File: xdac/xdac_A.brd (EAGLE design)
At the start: 100 x 80 mm, 76 parts, among them J1 LIWE_40_PIN, J12 FC68131, J3 PINHD-3X9/90, J34 FC68131, J4 PINHD-3X5/90, J56 FC68131, J78 FC68131, U1 STA311B, U2 CS4384, U3 FIN1002

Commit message: xdac: VIP
Signed-off-by: malo <pavol.malosek@gmail.com>
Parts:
- removed CKOUT, MUTEC_1, MUTEC_234: TPB1,27, testpad:B1,27
- removed J4: PINHD-3X5/90, 25pinhead:3X05/90
- removed R1: 220R, rcl:R0603
- removed R2, R3, R4, R5, R6: 470R, rcl:R0603
- removed U1: STA311B, 25cmsquare:VFQFPN_56_8X8
- C11, C12, C13, C14, C17, C18, C23, C24: device 25cmsquare:EEE-FC1V220P -> 25cmsquare:EEE-FC1C220R
- C15, C16, C19, C2, C20, C21, C22, C25, C26, C8, C9: device rcl:C0603K -> rcl:C0603
- J2: value (none) -> PINHD-3X5/90; device 25pinhead:3X08/90 -> 25pinhead:3X05/90
- J3: value PINHD-3X9/90 -> PINHD-3X5/90; device 25pinhead:3X9/90 -> 25pinhead:3X05/90
- moved R24 209.5 mm to (66.8, 20.1)
- moved C22 209.0 mm to (67.8, 30.5), turned to 270 degrees
- moved C21 204.2 mm to (67.8, 33.5), turned to 90 degrees
- moved R21 200.1 mm to (66.8, 27.9)
- moved R20 190.7 mm to (66.8, 36.1)
- moved C20 188.9 mm to (67.8, 62.5), turned to 270 degrees
- moved C16 188.1 mm to (67.8, 46.5), turned to 270 degrees
- moved C19 184.2 mm to (67.8, 65.5), turned to 90 degrees
- moved C15 183.4 mm to (67.8, 49.5), turned to 90 degrees
- moved R17 181.5 mm to (66.8, 43.9)
- moved C14 179.4 mm to (60.6, 45.1)
- moved R16 172.3 mm to (66.8, 52.1)
- moved R27 168.5 mm to (65.8, 14.5), turned to 270 degrees
- moved C13 167.9 mm to (60.6, 50.9)
- moved R13 163.4 mm to (66.8, 59.9)
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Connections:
- net CS_AOUT1 renamed AOUT1
- net CS_AOUT2 renamed AOUT2
- net CS_AOUT3 renamed AOUT3
- net CS_AOUT4 renamed AOUT4
- net CS_AOUT5 renamed AOUT5
- net CS_AOUT6 renamed AOUT6
- net CS_AOUT7 renamed AOUT7
- net CS_AOUT8 renamed AOUT8
- net N$13 renamed AUOT1_
- net N$14 renamed AOUT2_
- net N$23 renamed FILT+
- net N$25 renamed AOUT4_
- net N$26 renamed VQ
- net N$29 renamed AOUT3_
- net N$32 renamed AOUT6_
- net N$35 renamed AOUT5_
- net N$38 renamed AOUT8_
- net N$41 renamed AOUT7_
- removed net CS_DSD1: J2.10, U2.3
- removed net CS_DSD2: J2.12, U2.2
- removed net CS_DSD3: J2.13, U2.1
- removed net CS_DSD4: J2.15, U2.48
- removed net CS_DSD5: J2.16, U2.47
- removed net CS_DSD6: J2.18, U2.46
- removed net CS_DSD7: J2.19, U2.45
- removed net CS_DSD8: J2.21, U2.44
- removed net CS_DSD_CLK: J2.22, U2.42
- removed net CS_LRCLK: J2.3, R2.2, U2.7
- removed net CS_RST_N: J2.24, U2.19
- removed net CS_SCLK: J2.1, R1.2, U2.9
- removed net CS_SDIN1: J2.4, R3.2, U2.8
- removed net CS_SDIN2: J2.6, R4.2, U2.11
- removed net CS_SDIN3: J2.7, R5.2, U2.13
- removed net CS_SDIN4: J2.9, R6.2, U2.14
- removed net N$1: R1.1, U1.48
- removed net N$10: CKOUT.TP, U1.22
- removed net N$2: R2.1, U1.49
- removed net N$3: R3.1, U1.50
- removed net N$31: J4.15
- removed net N$4: R4.1, U1.51
- removed net N$43: J3.27
- removed net N$5: R5.1, U1.54
- removed net N$6: R6.1, U1.55
- removed net N$8: MUTEC_1.TP, U2.41
- removed net N$9: MUTEC_234.TP, U2.22
- removed net STA_1A: J3.1, U1.44
- removed net STA_1B: J3.3, U1.43
- removed net STA_2A: J3.4, U1.42
- removed net STA_2B: J3.6, U1.41
- removed net STA_3A: J3.7, U1.38
- removed net STA_3B: J3.9, U1.37
- removed net STA_4A: J3.10, U1.36
- removed net STA_4B: J3.12, U1.35
- removed net STA_5A: J3.13, U1.34
- removed net STA_5B: J3.15, U1.33
- removed net STA_6A: J3.16, U1.30
- removed net STA_6B: J3.18, U1.29
- removed net STA_7A: J3.19, U1.28
- removed net STA_7B: J3.21, U1.27
- removed net STA_8A: J3.22, U1.26
- removed net STA_8B: J3.24, U1.25
- removed net STA_BICKI: J4.1, U1.10
- removed net STA_EAPD: J3.25, U1.45
- removed net STA_LRCKI: J4.3, U1.9
- removed net STA_MVO: J4.10, U1.1
- removed net STA_PWDN: J4.13, U1.56
- removed net STA_RST_N: J4.12, U1.13
- removed net STA_SDI12: J4.4, U1.8
- removed net STA_SDI34: J4.6, U1.7
- removed net STA_SDI56: J4.7, U1.6
- removed net STA_SDI78: J4.9, U1.5
- new net DSD1: J2.3, U2.3
- new net DSD2: J2.1, U2.2
- new net DSD3: J2.6, U2.1
- new net DSD4: J2.4, U2.48
- new net DSD5: J2.9, U2.47
- new net DSD6: J2.7, U2.46
- new net DSD7: J2.12, U2.45
- new net DSD8: J2.10, U2.44
- new net DSD_CLK: J2.15, U2.42
- new net LRCLK: J3.3, U2.7
- new net MUTEC_1: J2.13, U2.41
- new net MUTEC_234: J3.15, U2.22
- new net RST_N: J3.12, U2.19
- new net SCLK: J3.1, U2.9
- new net SDIN1: J3.4, U2.8
- new net SDIN2: J3.6, U2.11
- new net SDIN3: J3.7, U2.13
- new net SDIN4: J3.9, U2.14
- net +3V3: no longer U1.11, U1.24, U1.3, U1.31, U1.39, U1.46, U1.52
- net 3V3A: no longer U1.21
- net GND: no longer J2.17, J2.20, J2.23, J3.17, J3.20, J3.23, J3.26, J4.11, J4.14, J4.2, J4.5, J4.8, U1.12, U1.14, U1.15, U1.2, U1.20, U1.23, U1.32, U1.4, U1.40, U1.47, U1.53, U1.PAD
- net MCLK: no longer U1.18
- net SCL: no longer U1.17
- net SDA: no longer U1.16
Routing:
- net GND: track 0.00 -> 59.6 mm
- net DSD1: track 0.00 -> 39.9 mm
- net DSD3: track 0.00 -> 37.8 mm
- net DSD7: track 0.00 -> 35.9 mm
- net DSD5: track 0.00 -> 35.8 mm
- net DSD_CLK: track 0.00 -> 35.1 mm
- net DSD2: track 0.00 -> 33.4 mm
- net AOUT1: track 0.00 -> 31.2 mm
- net AOUT8: track 0.00 -> 30.7 mm
- net DSD8: track 0.00 -> 30.5 mm
- net DSD4: track 0.00 -> 30.4 mm
- net DSD6: track 0.00 -> 30.1 mm
- net MUTEC_1: track 0.00 -> 30.0 mm
- net AOUT7: track 0.00 -> 26.4 mm
- net AOUT2: track 0.00 -> 25.3 mm
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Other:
- board size 100 x 80 mm -> 80 x 80 mm

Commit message: xdac: WIP
Signed-off-by: malo <pavol.malosek@gmail.com>
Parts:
- added JP1, JP3: (no value), 25pinhead:1X02/90
- C10: value 47u, EEEFC1V470P -> 47u, EEEFC0J470R; device 25cmsquare:EEE-FC1V470P -> 25cmsquare:EEE-FC1C220R
- C4, C5: device rcl:C0603K -> rcl:C0603
- moved C3 37.6 mm to (53.7, 40.0), turned to 90 degrees
- moved C30 31.2 mm to (14.9, 31.4), turned to 270 degrees
- moved C4 30.4 mm to (47.0, 40.7)
- moved C9 14.5 mm to (41.2, 32.2), turned to 270 degrees
- moved C10 13.7 mm to (40.3, 27.3), turned to 270 degrees
- moved C32 10.4 mm to (16.3, 23.1)
- moved C31 9.97 mm to (11.4, 23.0)
- moved JP2 9.47 mm to (11.2, 47.9), turned to 90 degrees
- moved FB2 8.90 mm to (13.6, 22.2)
- moved C7 7.91 mm to (45.9, 27.3), turned to 270 degrees
- moved C34 7.67 mm to (16.3, 14.8), turned to 270 degrees
- moved C15 7.41 mm to (72.8, 55.0), turned to 180 degrees
- moved C22 7.41 mm to (72.8, 25.0), turned to 180 degrees
- moved C19 7.41 mm to (72.8, 71.0), turned to 180 degrees
- moved C25 7.41 mm to (72.8, 23.0), turned to 180 degrees
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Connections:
- net GND: now also JP1.1, JP3.1
- net MUTEC_1: now also JP3.2; no longer J2.13
- net MUTEC_234: now also JP1.2; no longer J3.15
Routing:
- net 5VA: track 0.00 -> 192.0 mm
- net 3V3A: track 0.00 -> 80.3 mm, vias 0 -> 2
- net GND: track 59.6 -> 6.40 mm
- net +2V5: track 0.00 -> 51.0 mm
- net RST_N: track 1.53 -> 42.6 mm, vias 0 -> 2
- net SDIN1: track 0.00 -> 37.6 mm, vias 0 -> 2
- net SCLK: track 0.00 -> 36.2 mm, vias 0 -> 2
- net LRCLK: track 1.31 -> 33.1 mm, vias 0 -> 2
- net SDIN2: track 0.00 -> 31.5 mm, vias 0 -> 2
- net SDA: track 0.00 -> 23.3 mm, vias 0 -> 2
- net MCLK: track 0.00 -> 22.1 mm, vias 0 -> 2
- net SDIN3: track 0.00 -> 21.9 mm, vias 0 -> 2
- net SDIN4: track 0.00 -> 21.4 mm, vias 0 -> 2
- net SCL: track 0.00 -> 20.4 mm, vias 0 -> 2
- net +3V3: track 0.00 -> 20.1 mm, vias 0 -> 2
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
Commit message: xdac: VIP
Signed-off-by: malo <pavol.malosek@gmail.com>
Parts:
- removed JP2: (no value), 25pinhead:1X03
- added A1, A2, A3, A4, A5, A6, A7, A8, LRCLK, SCLK, SDIN1, SDIN2, SDIN3, SDIN4: (no value), 25pinhead:1X01
- added MCLK: (no value), 25pinhead:1X03
- added U$1, U$2, U$3, U$4, U$5, U$6: TEST-22-MULTICOMP, 25cmsquare:TEST_1MM
- moved C33 27.2 mm to (22.8, 25.3), turned to 270 degrees
- moved U3 26.7 mm to (25.8, 23.5), turned to 0 degrees
- moved R7 18.2 mm to (27.1, 29.0), turned to 270 degrees
- moved C30 17.9 mm to (16.7, 49.3), turned to 90 degrees
- moved C34 9.66 mm to (16.7, 24.4)
- moved C31 9.65 mm to (11.4, 32.6)
- moved FB2 9.60 mm to (14.2, 31.8)
- moved C32 9.56 mm to (16.7, 32.6)
- moved SDA 9.38 mm to (13.1, 56.2)
- moved JP3 7.24 mm to (56.3, 81.3)
- moved JP1 7.24 mm to (56.3, -1.32)
- moved SCL 6.07 mm to (13.1, 60.7)
- moved FB1 4.24 mm to (13.5, 40.8)
- moved C29 3.77 mm to (18.3, 40.0), turned to 270 degrees
- moved C28 3.32 mm to (16.2, 40.0), turned to 270 degrees
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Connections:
- removed net CLK2: J1.103, JP2.3, U3.3
- removed net CLK3: J1.104, JP2.1, U3.4
- new net CLK_N: J1.104, MCLK.1, U3.4
- new net CLK_P: J1.103, MCLK.3, U3.3
- net AOUT1: now also A1.1
- net AOUT2: now also A2.1
- net AOUT3: now also A3.1
- net AOUT4: now also A4.1
- net AOUT5: now also A5.1
- net AOUT6: now also A6.1
- net AOUT7: now also A7.1
- net AOUT8: now also A8.1
- net GND: now also U$1.1, U$2.1, U$3.1, U$4.1, U$5.1, U$6.1
- net LRCLK: now also J3.10, LRCLK.1; no longer J3.3
- net MCLK: now also MCLK.2; no longer JP2.2
- net RST_N: now also J3.3; no longer J3.12
- net SCLK: now also J3.7, SCLK.1; no longer J3.1
- net SDIN1: now also J3.9, SDIN1.1; no longer J3.4
- net SDIN2: now also SDIN2.1
- net SDIN3: now also J3.4, SDIN3.1; no longer J3.7
- net SDIN4: now also J3.1, SDIN4.1; no longer J3.9
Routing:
- net CLK_N: track 0.00 -> 74.9 mm
- net CLK_P: track 0.00 -> 74.8 mm
- net SCL: track 20.4 -> 63.0 mm
- net SDA: track 23.3 -> 59.0 mm
- net 5VA: track 192.0 -> 164.9 mm
- net +3V3: track 20.1 -> 46.2 mm, vias 2 -> 0
- net DSD_CLK: track 17.9 -> 36.3 mm
- net 3V3A: track 80.3 -> 67.2 mm, vias 2 -> 0
- net SDIN3: track 21.9 -> 34.0 mm, vias 2 -> 1
- net SDIN4: track 21.4 -> 33.4 mm, vias 2 -> 1
- net SDIN2: track 31.5 -> 43.1 mm, vias 2 -> 1
- net MCLK: track 22.1 -> 31.3 mm
- net MUTEC_1: track 32.0 -> 40.1 mm
- net AOUT1: track 25.9 -> 33.4 mm
- net +2V5: track 51.0 -> 43.5 mm, vias 0 -> 2
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- added copper zone on layer 1, net 3V3A
- added copper zone on layer 1, net 5VA
- added copper zone on layer 1, net GND
- added copper zone on layer 16, net GND

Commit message: xdac: VIP
Signed-off-by: malo <pavol.malosek@gmail.com>
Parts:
- added +5V, 2V5, 3V3: TPTP14R, testpad:TP14R
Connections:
- net +2V5: now also 2V5.TP
- net +3V3: now also 3V3.TP
- net +5V: now also +5V.TP
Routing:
- net +2V5: track 43.5 -> 45.6 mm
- net +5V: track 9.04 -> 10.7 mm
- net +3V3: track 46.2 -> 47.7 mm
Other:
- board text added: "17.03.27.A"
- board text added: "GND"
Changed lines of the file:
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@@
 <?xml version="1.0" encoding="utf-8"?>
 <!DOCTYPE eagle SYSTEM "eagle.dtd">
-<eagle version="8.1.0">
+<eagle version="7.7.0">
 <drawing>
 <settings>
@@
 <setting verticaltext="up"/>
 </settings>
-<grid distance="10" unitdist="mil" unit="mil" style="lines" multiple="1" display="yes" altdistance="0.025" altunitdist="inch" altunit="inch"/>
+<grid distance="1" unitdist="mil" unit="mil" style="lines" multiple="1" display="yes" altdistance="0.025" altunitdist="inch" altunit="inch"/>
 <layers>
 <layer number="1" name="Top" color="4" fill="1" visible="yes" active="yes"/>
@@
 <board>
 <plain>
+<text x="16.6624" y="77.1652" size="2.032" layer="25" font="vector" ratio="15" align="bottom-center">17.03.27.A</text>
+<text x="64.9224" y="74.1172" size="1.016" layer="25" font="vector" ratio="15" align="bottom-center">GND</text>
+<text x="64.9224" y="4.5212" size="1.016" layer="25" font="vector" ratio="15" align="bottom-center">GND</text>
+<text x="17.4244" y="4.5212" size="1.016" layer="25" font="vector" ratio="15" align="bottom-center">GND</text>
 </plain>
 <attributes>
@@
 <element name="U$5" library="25cmsquare" package="TEST_1MM" value="TEST-22-MULTICOMP" x="13.589" y="5.1562" smashed="yes"/>
 <element name="U$6" library="25cmsquare" package="TEST_1MM" value="TEST-22-MULTICOMP" x="21.082" y="5.1562" smashed="yes"/>
+<element name="2V5" library="testpad" package="TP14R" value="TPTP14R" x="20.1676" y="34.2138" smashed="yes">
+<attribute name="TP_SIGNAL_NAME" value="" x="20.1676" y="31.6738" size="1" layer="37"/>
+<attribute name="NAME" x="21.144" y="33.7955" size="1.016" layer="25" font="vector" ratio="15"/>
+</element>
+<element name="3V3" library="testpad" package="TP14R" value="TPTP14R" x="16.0782" y="15.113" smashed="yes">
+<attribute name="TP_SIGNAL_NAME" value="" x="16.0782" y="12.573" size="1" layer="37"/>
+<attribute name="NAME" x="14.7432" y="13.1199" size="1.016" layer="25" font="vector" ratio="15"/>
+</element>
+<element name="+5V" library="testpad" package="TP14R" value="TPTP14R" x="9.4742" y="42.4434" smashed="yes">
+<attribute name="TP_SIGNAL_NAME" value="" x="9.4742" y="39.9034" size="1" layer="37"/>
+<attribute name="NAME" x="8.2916" y="43.3205" size="1.016" layer="25" font="vector" ratio="15"/>
+</element>
 </elements>
 <signals>
@@
 <wire x1="25.6794" y1="17.907" x2="26.1366" y2="18.3642" width="0.1524" layer="1"/>
 <wire x1="25.6794" y1="17.907" x2="25.6794" y2="15.494" width="0.1524" layer="1"/>
-<wire x1="26.1366" y1="29.7434" x2="26.289" y2="29.8958" width="0.1524" layer="1"/>
-<wire x1="26.289" y1="29.8958" x2="27.0628" y2="29.8958" width="0.1524" layer="1"/>
+<wire x1="26.0858" y1="29.8958" x2="27.0628" y2="29.8958" width="0.1524" layer="1"/>
 <wire x1="27.0628" y1="29.8958" x2="27.0764" y2="29.8822" width="0.1524" layer="1"/>
-<wire x1="26.1366" y1="18.3642" x2="26.1366" y2="29.7434" width="0.1524" layer="1"/>
+<wire x1="26.1366" y1="18.3642" x2="26.1366" y2="26.6954" width="0.1524" layer="1"/>
 <wire x1="32.5284" y1="40.25" x2="27.0764" y2="34.798" width="0.1524" layer="1"/>
 <wire x1="35.75" y1="40.25" x2="32.5284" y2="40.25" width="0.1524" layer="1"/>
+<wire x1="26.1366" y1="26.6954" x2="25.908" y2="26.924" width="0.1524" layer="1"/>
+<wire x1="25.908" y1="26.924" x2="25.908" y2="29.718" width="0.1524" layer="1"/>
+<wire x1="25.908" y1="29.718" x2="26.0858" y2="29.8958" width="0.1524" layer="1"/>
 </signal>
 <signal name="GND">
@@
 <wire x1="3.8508" y1="35.3976" x2="3.8508" y2="35.4200125" width="0.6096" layer="1"/>
 <wire x1="3.8508" y1="35.4200125" x2="4.6257875" y2="36.195" width="0.6096" layer="1"/>
-<wire x1="4.6257875" y1="36.195" x2="22.5044" y2="36.195" width="0.6096" layer="1"/>
+<wire x1="4.6257875" y1="36.195" x2="20.1422" y2="36.195" width="0.6096" layer="1"/>
+<wire x1="20.1422" y1="36.195" x2="22.5044" y2="36.195" width="0.6096" layer="1"/>
 <wire x1="22.5044" y1="36.195" x2="23.0124" y2="36.703" width="0.6096" layer="1"/>
 <wire x1="23.0124" y1="36.703" x2="23.0124" y2="42.926" width="0.6096" layer="1"/>
@@
 <via x="26.0858" y="42.926" extent="1-16" drill="0.6" shape="square"/>
 <wire x1="28.5242" y1="42.926" x2="26.0858" y2="42.926" width="0.6096" layer="1"/>
+<contactref element="2V5" pad="TP"/>
+<wire x1="20.1676" y1="34.2138" x2="20.1422" y2="34.2138" width="0.1524" layer="1"/>
+<wire x1="20.1422" y1="34.2138" x2="20.1422" y2="36.195" width="0.1524" layer="1"/>
 </signal>
 <signal name="+5V">
@@
 <wire x1="11.176" y1="40.8038" x2="11.1746" y2="40.8078" width="0.2032" layer="1"/>
 <wire x1="11.176" y1="40.8038" x2="11.152" y2="40.7824" width="0.6096" layer="1"/>
-<wire x1="11.152" y1="40.7824" x2="8.3974" y2="40.7824" width="0.6096" layer="1"/>
+<wire x1="11.152" y1="40.7824" x2="9.4488" y2="40.7824" width="0.6096" layer="1"/>
+<wire x1="9.4488" y1="40.7824" x2="8.3974" y2="40.7824" width="0.6096" layer="1"/>
 <wire x1="8.3974" y1="40.7824" x2="5.07" y2="37.455" width="0.6096" layer="1"/>
 <wire x1="12.7128" y1="40.8178" x2="11.19" y2="40.8178" width="0.6096" layer="1"/>
 <wire x1="11.19" y1="40.8178" x2="11.176" y2="40.8038" width="0.6096" layer="1"/>
+<contactref element="+5V" pad="TP"/>
+<wire x1="9.4742" y1="42.4434" x2="9.4488" y2="42.4434" width="0.1524" layer="1"/>
+<wire x1="9.4488" y1="42.4434" x2="9.4488" y2="40.7824" width="0.1524" layer="1"/>
 </signal>
 <signal name="+3V3">
@@
 <wire x1="13.424" y1="31.7754" x2="11.4046" y2="31.7754" width="0.6096" layer="1"/>
 <wire x1="11.4046" y1="17.653" x2="12.3952" y2="16.6624" width="0.6096" layer="1"/>
-<wire x1="12.3952" y1="16.6624" x2="19.8882" y2="16.6624" width="0.6096" layer="1"/>
+<wire x1="12.3952" y1="16.6624" x2="16.0782" y2="16.6624" width="0.6096" layer="1"/>
+<wire x1="16.0782" y1="16.6624" x2="19.8882" y2="16.6624" width="0.6096" layer="1"/>
 <wire x1="22.7838" y1="24.4738" x2="22.7584" y2="24.4484" width="0.6096" layer="1"/>
 <wire x1="11.4046" y1="31.7754" x2="11.4046" y2="17.653" width="0.6096" layer="1"/>
@@
 <wire x1="21.59" y1="24.4602" x2="22.7702" y2="24.4602" width="0.6096" layer="1"/>
 <wire x1="22.7702" y1="24.4602" x2="22.7838" y2="24.4738" width="0.6096" layer="1"/>
+<contactref element="3V3" pad="TP"/>
+<wire x1="16.0782" y1="15.113" x2="16.0782" y2="16.6624" width="0.1524" layer="1"/>
 </signal>
 <signal name="VQ">

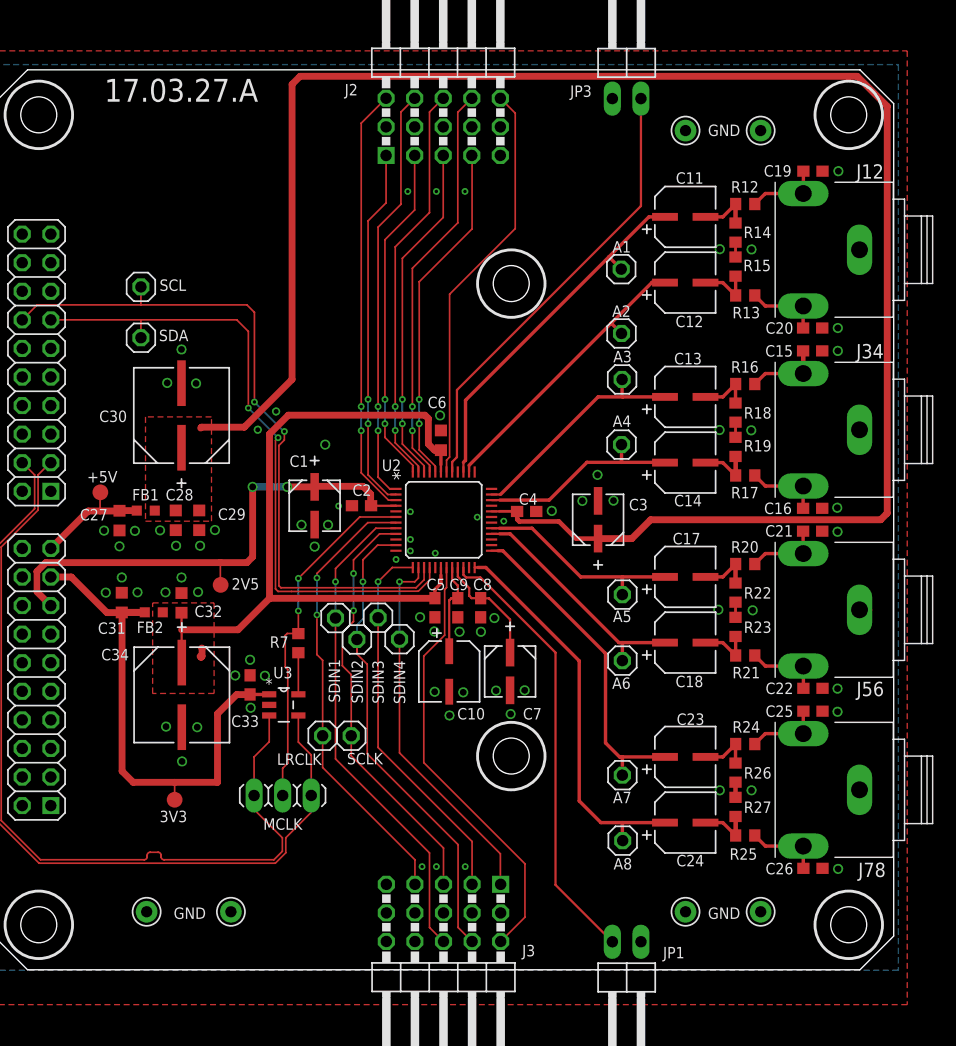
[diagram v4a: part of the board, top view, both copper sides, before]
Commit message: xdac: finished PCB
Signed-off-by: malo <pavol.malosek@gmail.com>
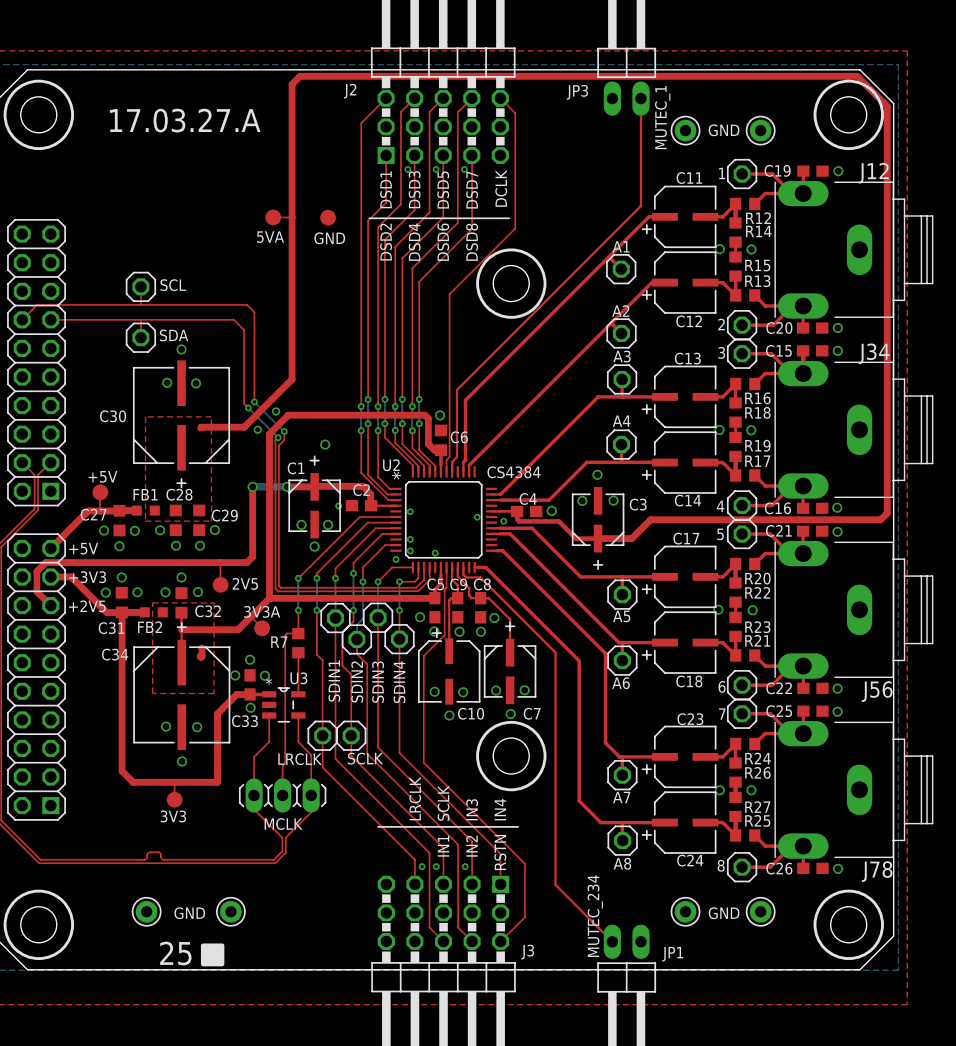
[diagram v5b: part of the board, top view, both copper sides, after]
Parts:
- added 1, 2, 3, 4, 5, 6, 7, 8: (no value), 25pinhead:1X01
- added 3V3A, 5VA, GND___: TPTP14R, testpad:TP14R
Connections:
- net 3V3A: now also 3V3A.TP
- net 5VA: now also 5VA.TP
- net AOUT2_: now also 2.1
- net AOUT3_: now also 3.1
- net AOUT4_: now also 4.1
- net AOUT5_: now also 5.1
- net AOUT6_: now also 6.1
- net AOUT7_: now also 7.1
- net AOUT8_: now also 8.1
- net AUOT1_: now also 1.1
- net GND: now also GND___.TP
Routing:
- net AUOT1_: track 6.70 -> 11.6 mm
- net AOUT2_: track 6.66 -> 11.6 mm
- net AOUT8_: track 6.68 -> 11.6 mm
- net AOUT4_: track 6.69 -> 11.6 mm
- net AOUT3_: track 6.72 -> 11.6 mm
- net AOUT7_: track 6.70 -> 11.5 mm
- net AOUT6_: track 6.69 -> 11.5 mm
- net AOUT5_: track 6.69 -> 11.4 mm
- net 5VA: track 164.9 -> 166.6 mm
- net 3V3A: track 67.2 -> 68.6 mm
- net SDIN4: vias 1 -> 2
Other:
- board text added: "+2V5"
- board text added: "+3V3"
- board text added: "+5V"
- board text added: "25"
- board text added: "CS4384"
- board text added: "DCLK"
- board text added: "DSD1"
- board text added: "DSD2"
- board text added: "DSD3"
- board text added: "DSD4"
- board text added: "DSD5"
- board text added: "DSD6"
- board text added: "DSD7"
- board text added: "DSD8"
- board text added: "IN1"
- board text added: "IN2"
- board text added: "IN3"
- board text added: "IN4"
- board text added: "LRCLK"
- board text added: "MUTEC_1"
- board text added: "MUTEC_234"
- board text added: "RSTN"
- board text added: "SCLK"
